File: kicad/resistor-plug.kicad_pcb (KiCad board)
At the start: 2 copper layers, 27.9 x 6.4 mm, 6 parts

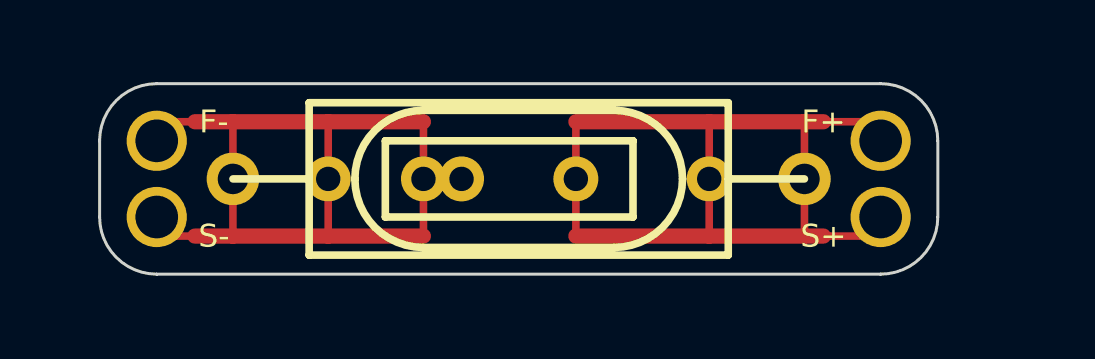
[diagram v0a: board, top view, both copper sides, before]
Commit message: adding flood fill
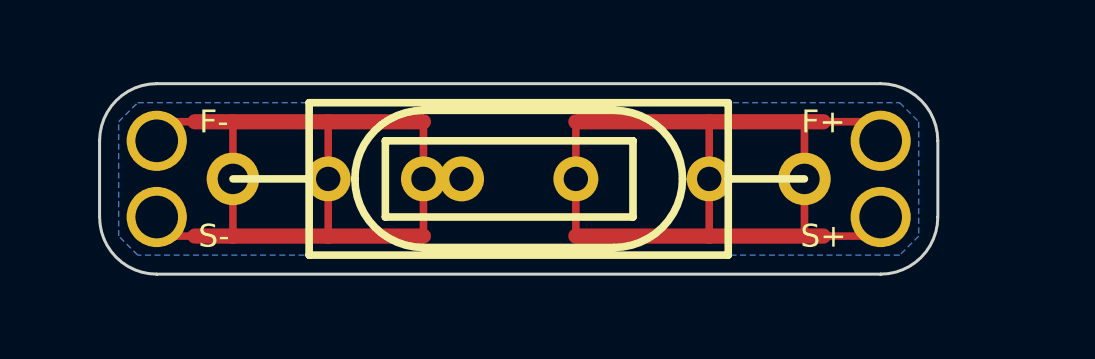
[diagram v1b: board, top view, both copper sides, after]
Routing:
- added copper zone on B.Cu, net (none)
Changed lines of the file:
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@@
     (links 0)
     (no_connects 0)
-    (area 156.463999 75.183999 241.751555 128.651001)
+    (area 153.641778 91.821 184.178222 101.219)
     (thickness 1.6)
     (drawings 12)
@@
   (segment (start 162.56 94.615) (end 159.385 94.615) (width 0.508) (layer F.Cu) (net 0))
   (segment (start 159.385 98.425) (end 162.56 98.425) (width 0.508) (layer F.Cu) (net 0))
+  (zone (net 0) (net_name "") (layer B.Cu) (hatch edge 0.508)
+    (connect_pads (clearance 0.508))
+    (min_thickness 0.254)
+    (fill (arc_segments 16) (thermal_gap 0.508) (thermal_bridge_width 0.508))
+    (polygon
+      (pts
+        (xy 182.245 98.425) (xy 181.61 99.06) (xy 156.21 99.06) (xy 155.575 98.425) (xy 155.575 94.615)
+        (xy 156.21 93.98) (xy 181.61 93.98) (xy 182.245 94.615)
+      )
+    )
+  )
 )

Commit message: v1.1
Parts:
- removed H*** (x4): Val**, 1pin_056_079
- removed R***: VAL**, R_BOX_HERMETIC_AXIAL_05_PL
- removed R***: VAL**, R_AXIAL_WW_069A_075_PL
- added P1: CONN_1X1, 1pin_056_079, F.Cu at (156.8, 96.5)
- added P2: CONN_1X1, 1pin_056_079, F.Cu at (183.5, 95.2)
- added P3: CONN_1X1, 1pin_056_079, F.Cu at (181.0, 97.8)
- added P4: CONN_1X1, 1pin_056_079, F.Cu at (183.5, 97.8)
- added P5: CONN_1X1, 1pin_056_079, F.Cu at (181.0, 95.2)
- added R1: R, R_BOX_HERMETIC_AXIAL_05_PL, F.Cu at (168.9, 96.5)
- added R2: R, R_AXIAL_WW_069A_075_PL, F.Cu at (159.4, 96.5)
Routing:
- net N-000003: track 0.00 -> 66.1 mm
- net (no net): track 62.0 -> 0.00 mm
- net N-000001: track 0.00 -> 27.9 mm
- added copper zone on B.Cu, net GND
- added copper zone on F.Cu, net GND
- removed copper zone on B.Cu, net (none)
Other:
- board outline removed
- board text added: "Resistor plug v1.1"
- board text added: "github.com/pepaslabs/resistor-plug"

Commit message: v1.1
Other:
- board outline added: 32.4 x 7.6 mm
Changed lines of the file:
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@@
     (links 9)
     (no_connects 0)
-    (area 0 0 0 0)
+    (area 151.948445 91.821 188.411555 101.219)
     (thickness 1.6)
-    (drawings 6)
+    (drawings 14)
     (tracks 34)
     (zones 0)
@@
     )
   )
+  (gr_line (start 153.67 99.695) (end 153.67 93.345) (angle 90) (layer Edge.Cuts) (width 0.1))
+  (gr_line (start 185.42 100.33) (end 154.305 100.33) (angle 90) (layer Edge.Cuts) (width 0.1))
+  (gr_line (start 186.055 93.345) (end 186.055 99.695) (angle 90) (layer Edge.Cuts) (width 0.1))
+  (gr_line (start 154.305 92.71) (end 185.42 92.71) (angle 90) (layer Edge.Cuts) (width 0.1))
+  (gr_arc (start 154.305 93.345) (end 153.67 93.345) (angle 90) (layer Edge.Cuts) (width 0.1))
+  (gr_arc (start 154.305 99.695) (end 154.305 100.33) (angle 90) (layer Edge.Cuts) (width 0.1))
+  (gr_arc (start 185.42 99.695) (end 186.055 99.695) (angle 90) (layer Edge.Cuts) (width 0.1))
+  (gr_arc (start 185.42 93.345) (end 185.42 92.71) (angle 90) (layer Edge.Cuts) (width 0.1))
   (gr_text "Resistor plug v1.1" (at 178.435 93.98) (layer B.SilkS)
     (effects (font (size 0.762 0.762) (thickness 0.1524)) (justify left mirror))
